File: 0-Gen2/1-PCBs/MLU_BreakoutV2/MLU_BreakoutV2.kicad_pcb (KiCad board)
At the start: 4 copper layers, 129.3 x 99 mm, 151 parts, among them J11 430450422, J12 PixHawk PM02, J13 SBH11-PBPC-D10-ST-BK, J14 Conn_01x02_Socket, J17 430450422, J18 430450422, J19 430450422, J2 430450422, J20 430450228, J21 430450228, J22 430450228, J23 430450228, J25 430450228, J26 430450821, J28 Conn_01x04_Socket, J3 Conn_01x03_Pin, J3 J1B1211CCD, J31 Conn_01x02_Socket, J4 430450422, J4 Conn_02x03_Odd_Even, J5 430451027, J6 430450228, J7 SBH11-PBPC-D10-ST-BK, J8 Conn_02x22_Odd_Even, SW1 09.03201.02, U1 Teensy4.1, U17 BA033CC0FP-E2, U2 MCP9808_MSOP, U3 MCP9808_MSOP, U4 BME280, U7 MCP23008-E_P

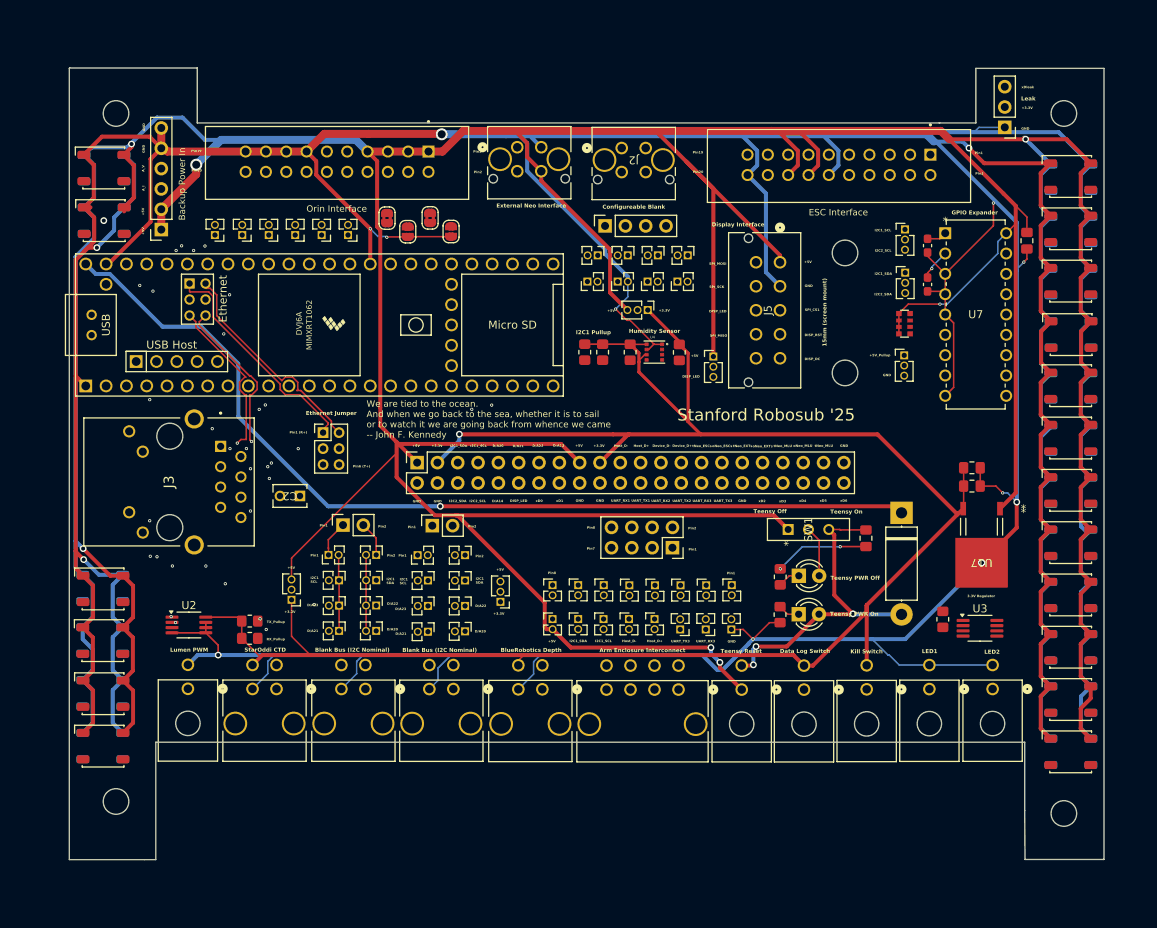
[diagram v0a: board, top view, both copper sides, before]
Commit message: [bugfix] rescued footprints
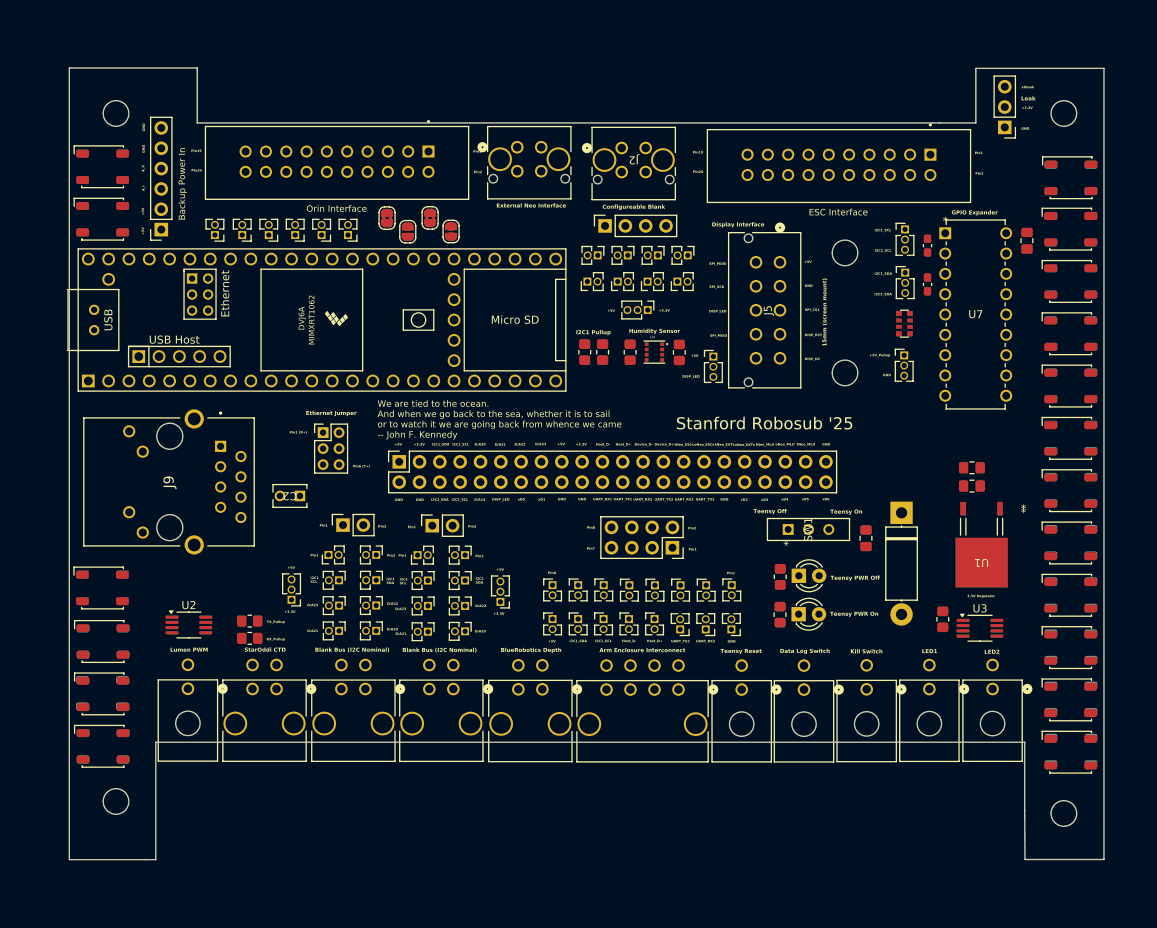
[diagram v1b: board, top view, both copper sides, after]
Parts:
- LED1, LED2: moved to F.Cu
- LED19, LED36: moved to B.Cu
- moved LED31 141.4 mm to (130.0, 63.6)
- moved LED7 140.3 mm to (251.1, 65.0)
- moved LED36 131.5 mm to (130.1, 136.0), turned to 180 degrees
- moved LED11 122.6 mm to (251.0, 91.0)
- moved LED19 71.7 mm to (251.0, 65.0), turned to 180 degrees
- moved LED5 65.7 mm to (130.1, 129.5)
- moved LED32 46.1 mm to (130.0, 70.2)
- moved LED35 6.60 mm to (130.0, 129.4)
- moved LED10 6.58 mm to (251.0, 84.5)
- moved LED12 6.58 mm to (251.0, 97.5)
- moved LED14 6.58 mm to (251.0, 110.6)
- moved LED15 6.58 mm to (251.0, 117.2)
- moved LED18 6.58 mm to (251.0, 136.8)
- moved LED9 6.58 mm to (251.0, 77.9)
- moved LED13 6.58 mm to (251.0, 104.1)
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- renumbered J4 to J10, J3 to J9, U17 to U1, U1 to U6
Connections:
- J8 pad 22: UART_RX1 -> UART_TX1
- J8 pad 24: UART_TX1 -> UART_RX1
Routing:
- net GND: track 845.7 -> 0.00 mm, vias 18 -> 0
- net +5V: track 807.3 -> 0.00 mm, vias 7 -> 0
- net +3.3V: track 248.8 -> 0.00 mm, vias 1 -> 0
- net Teensy_5V: track 118.7 -> 0.00 mm, vias 1 -> 0
- net D/A22: track 88.1 -> 0.00 mm, vias 5 -> 0
- net D/A23: track 81.6 -> 0.00 mm, vias 3 -> 0
- net D/A21: track 79.3 -> 0.00 mm, vias 2 -> 0
- net I2C1_SDA: track 76.0 -> 0.00 mm, vias 2 -> 0
- net D/A20: track 69.1 -> 0.00 mm, vias 2 -> 0
- net UART_RX2: track 65.8 -> 0.00 mm, vias 3 -> 0
- net I2C1_SCL: track 65.4 -> 0.00 mm, vias 4 -> 0
- net UART_TX2: track 64.6 -> 0.00 mm, vias 3 -> 0
- net Lumen_PWM: track 43.8 -> 0.00 mm
- net R-: track 43.5 -> 0.00 mm
- net R+: track 42.3 -> 0.00 mm
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
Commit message: before renumbering LEDs
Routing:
- net GND: track 0.00 -> 125.7 mm, vias 0 -> 30
- net +5V: track 0.00 -> 54.4 mm, vias 0 -> 18
- net +3.3V: track 0.00 -> 26.1 mm, vias 0 -> 9
- added copper zone on In2.Cu, net +3.3V
- added copper zone on F.Cu, net +5V
- added copper zone on In1.Cu, net GND

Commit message: routing
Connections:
- LED1 pad 2: NEO_PASS7 -> toNEO_CTRL_MLU
- LED11 pad 2: Net-(LED11-DIN) -> Net-(LED10-DOUT)
- LED12 pad 2: Net-(LED12-DIN) -> Net-(LED11-DOUT)
- LED12 pad 4: Net-(LED12-DOUT) -> NEO_PASS3
- LED13 pad 2: Net-(LED13-DIN) -> NEO_PASS3
- LED14 pad 2: Net-(LED14-DIN) -> Net-(LED13-DOUT)
- LED15 pad 2: Net-(LED15-DIN) -> Net-(LED14-DOUT)
- LED16 pad 2: Net-(LED10-DOUT) -> Net-(LED15-DOUT)
- LED16 pad 4: Net-(LED16-DOUT) -> NEO_PASS4
- LED17 pad 2: Net-(LED11-DOUT) -> NEO_PASS4
- LED18 pad 2: Net-(LED12-DOUT) -> Net-(LED17-DOUT)
- LED19 pad 2: Net-(LED13-DOUT) -> Net-(LED18-DOUT)
- LED19 pad 4: NEO_PASS8 -> Net-(LED19-DOUT)
- LED2 pad 2: NEO_PASS6 -> Net-(LED1-DOUT)
- LED20 pad 2: Net-(LED14-DOUT) -> Net-(LED19-DOUT)
- LED20 pad 4: NEO_PASS7 -> NEO_PASS5
- LED21 pad 2: Net-(LED15-DOUT) -> NEO_PASS5
- LED21 pad 4: outNEO_CTRL_MLU -> Net-(LED21-DOUT)
- LED22 pad 2: Net-(LED16-DOUT) -> Net-(LED21-DOUT)
- LED22 pad 4: NEO_PASS2 -> Net-(LED22-DOUT)
- LED23 pad 2: Net-(LED17-DOUT) -> Net-(LED22-DOUT)
- LED23 pad 4: NEO_PASS1 -> Net-(LED23-DOUT)
- LED24 pad 2: Net-(LED18-DOUT) -> Net-(LED23-DOUT)
- LED24 pad 4: NEO_PASS3 -> NEO_PASS6
- LED25 pad 2: NEO_PASS4 -> NEO_PASS6
- LED26 pad 2: NEO_PASS3 -> Net-(LED25-DOUT)
- LED27 pad 2: NEO_PASS5 -> Net-(LED26-DOUT)
- LED28 pad 2: Net-(LED25-DOUT) -> Net-(LED27-DOUT)
- LED28 pad 4: Net-(LED28-DOUT) -> NEO_PASS7
- LED29 pad 2: Net-(LED26-DOUT) -> NEO_PASS7
- LED3 pad 2: NEO_PASS8 -> Net-(LED2-DOUT)
- LED30 pad 2: Net-(LED27-DOUT) -> Net-(LED29-DOUT)
- LED31 pad 2: Net-(LED28-DOUT) -> Net-(LED30-DOUT)
- LED32 pad 2: Net-(LED29-DOUT) -> Net-(LED31-DOUT)
- LED32 pad 4: Net-(LED32-DOUT) -> NEO_PASS8
- LED33 pad 2: Net-(LED30-DOUT) -> NEO_PASS8
- LED34 pad 2: Net-(LED31-DOUT) -> Net-(LED33-DOUT)
- LED34 pad 4: NEO_PASS5 -> Net-(LED34-DOUT)
- LED35 pad 2: Net-(LED32-DOUT) -> Net-(LED34-DOUT)
- LED35 pad 4: NEO_PASS4 -> Net-(LED35-DOUT)
- LED36 pad 2: Net-(LED33-DOUT) -> Net-(LED35-DOUT)
- LED36 pad 4: NEO_PASS6 -> outNEO_CTRL_MLU
- LED4 pad 2: NEO_PASS1 -> Net-(LED3-DOUT)
- LED4 pad 4: Net-(LED10-DIN) -> NEO_PASS1
- LED5 pad 2: toNEO_CTRL_MLU -> NEO_PASS1
- LED5 pad 4: Net-(LED11-DIN) -> Net-(LED5-DOUT)
- LED6 pad 2: NEO_PASS2 -> Net-(LED5-DOUT)
- LED6 pad 4: Net-(LED12-DIN) -> Net-(LED6-DOUT)
- LED7 pad 2: Net-(LED1-DOUT) -> Net-(LED6-DOUT)
- LED7 pad 4: Net-(LED13-DIN) -> Net-(LED7-DOUT)
- LED8 pad 2: Net-(LED2-DOUT) -> Net-(LED7-DOUT)
- LED8 pad 4: Net-(LED14-DIN) -> NEO_PASS2
- LED9 pad 2: Net-(LED3-DOUT) -> NEO_PASS2
- LED9 pad 4: Net-(LED15-DIN) -> Net-(LED10-DIN)
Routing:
- net Teensy_5V: track 0.00 -> 135.6 mm
- net I2C1_SCL: track 0.00 -> 80.2 mm, vias 0 -> 3
- net I2C1_SDA: track 0.00 -> 76.9 mm, vias 0 -> 3
- net ETH_GND: track 0.00 -> 61.7 mm, vias 0 -> 2
- net UART_RX2: track 0.00 -> 54.9 mm, vias 0 -> 3
- net Net-(LED2-DOUT): track 0.00 -> 53.5 mm, vias 0 -> 2
- net UART_TX2: track 0.00 -> 53.0 mm, vias 0 -> 3
- net NEO_PASS8: track 0.00 -> 49.3 mm
- net R-: track 0.00 -> 47.8 mm, vias 0 -> 3
- net R+: track 0.00 -> 47.6 mm, vias 0 -> 3
- net LED: track 0.00 -> 46.2 mm, vias 0 -> 5
- net Lumen_PWM: track 0.00 -> 45.3 mm, vias 0 -> 3
- net Net-(D1-A): track 0.00 -> 38.5 mm
- net T+: track 0.00 -> 37.2 mm, vias 0 -> 3
- net T-: track 0.00 -> 36.6 mm, vias 0 -> 4
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
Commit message: initial routing done
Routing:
- net I2C1_SCL: track 80.2 -> 329.5 mm, vias 3 -> 32
- net I2C1_SDA: track 76.9 -> 319.5 mm, vias 3 -> 29
- net Net-(LED30-DOUT): track 0.00 -> 187.3 mm, vias 0 -> 2
- net Net-(LED6-DOUT): track 0.00 -> 178.9 mm, vias 0 -> 4
- net outNEO_CTRL_MLU: track 0.00 -> 118.6 mm, vias 0 -> 6
- net Dswitch2: track 0.00 -> 107.1 mm, vias 0 -> 13
- net D/A22: track 0.00 -> 103.1 mm, vias 0 -> 14
- net D/A21: track 0.00 -> 103.0 mm, vias 0 -> 9
- net Host_D-: track 0.00 -> 93.2 mm, vias 0 -> 8
- net Dled2: track 0.00 -> 92.9 mm
- net D/A23: track 0.00 -> 91.6 mm, vias 0 -> 24
- net Host_D+: track 0.00 -> 91.0 mm, vias 0 -> 9
- net Dled1: track 0.00 -> 89.2 mm
- net D/A20: track 0.00 -> 83.9 mm, vias 0 -> 12
- net Net-(LED18-DOUT): track 0.00 -> 83.7 mm, vias 0 -> 1
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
